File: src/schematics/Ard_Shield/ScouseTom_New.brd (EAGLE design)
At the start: 129.7 x 53.7 mm, 64 parts, among them IC1 LM317MBDT, IC2 AD5280, J1 Stim out Brd, J2 STIM OUT, Q1 FDV303N, Q2 BC817, Q3 FDN304P, U1 ADUM5402ARWZ, U2 ADM3202ARUZ, U3 ADUM5000ARWZ, U4 ADUM1410ARWZ, U5 ADUM1410ARWZ

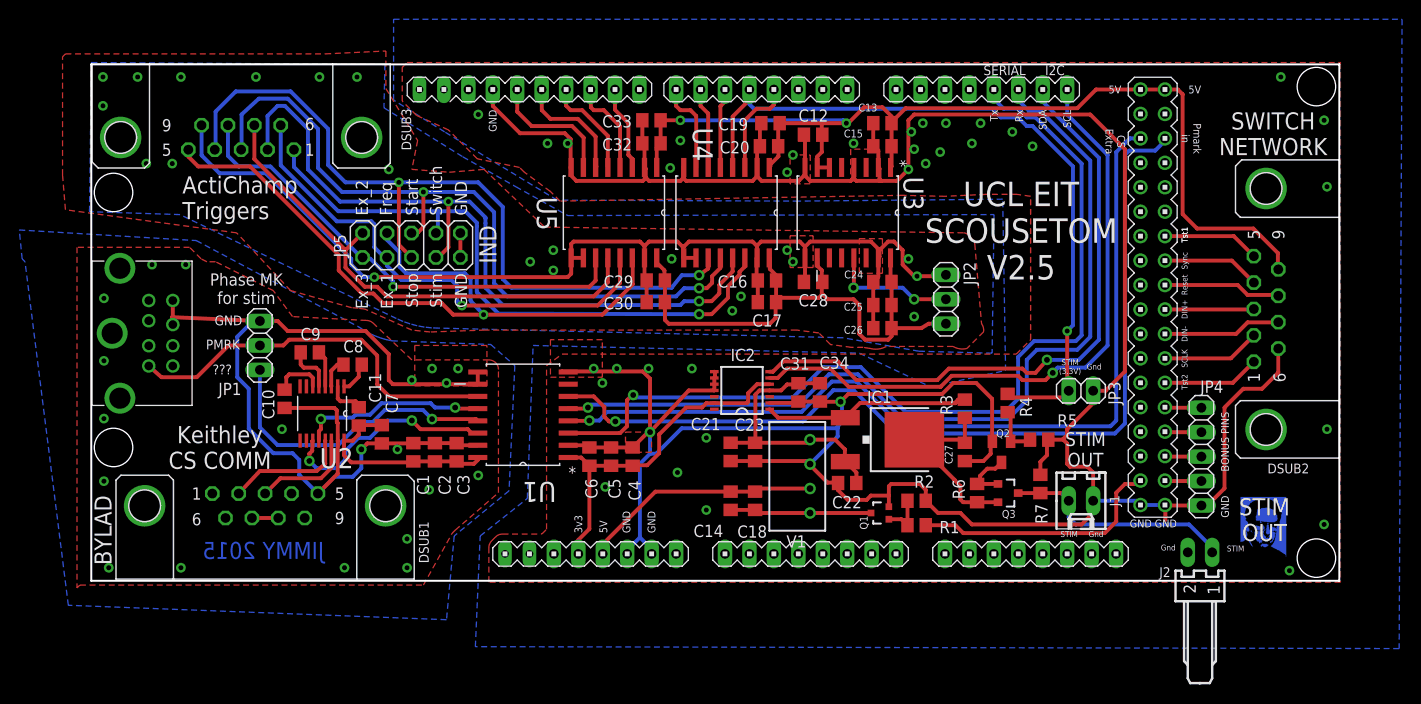
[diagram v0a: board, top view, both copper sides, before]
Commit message: Updated ScouseTom Shield SilkScreen and Gerber for PCB train order
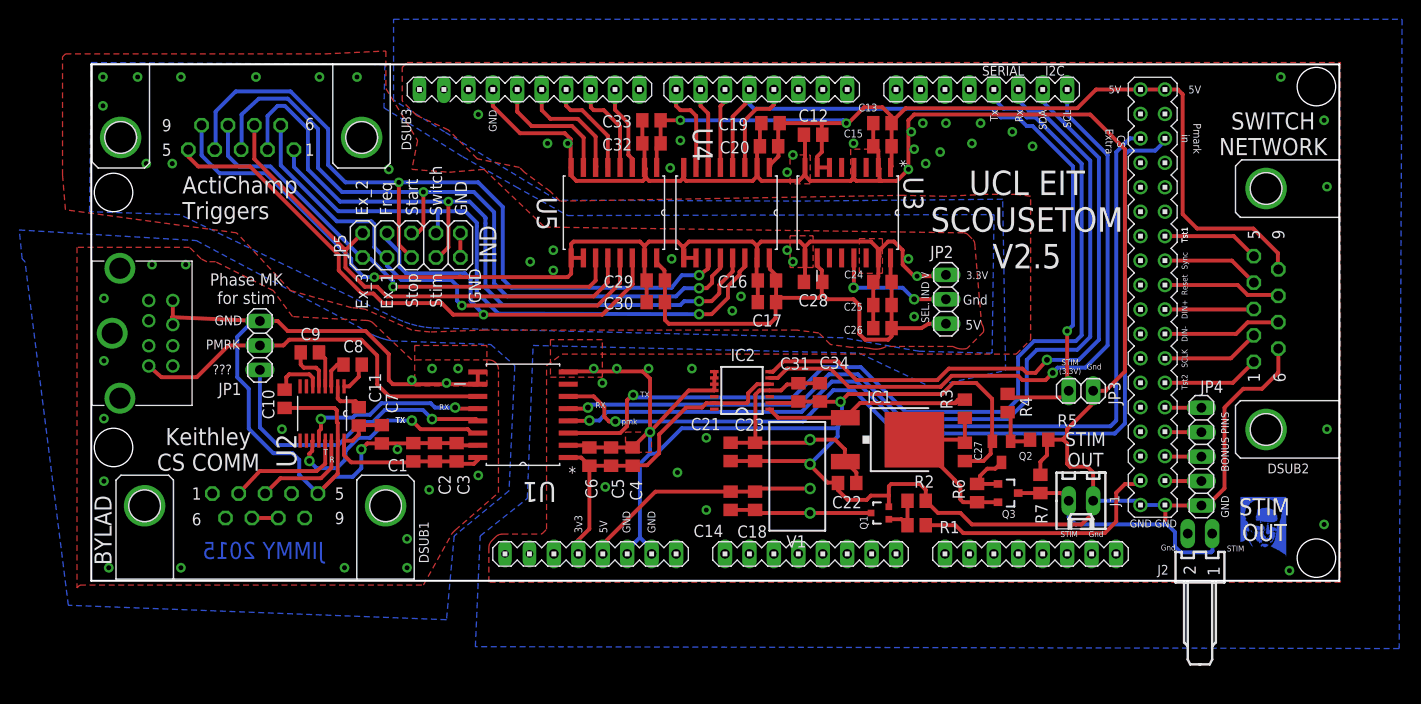
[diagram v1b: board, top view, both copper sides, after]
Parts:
- moved J2 1.95 mm to (99.9, 18.6)
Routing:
- net STIM_OUT: track 24.0 -> 26.5 mm
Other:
- board text added: "3.3V"
- board text added: "R"
- board text added: "RX"
- board text added: "SEL. IND V"
- board text added: "T"
- board text added: "TX"
- board text added: "pmk"

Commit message: CS extra pin added. Fixed angles on tracks
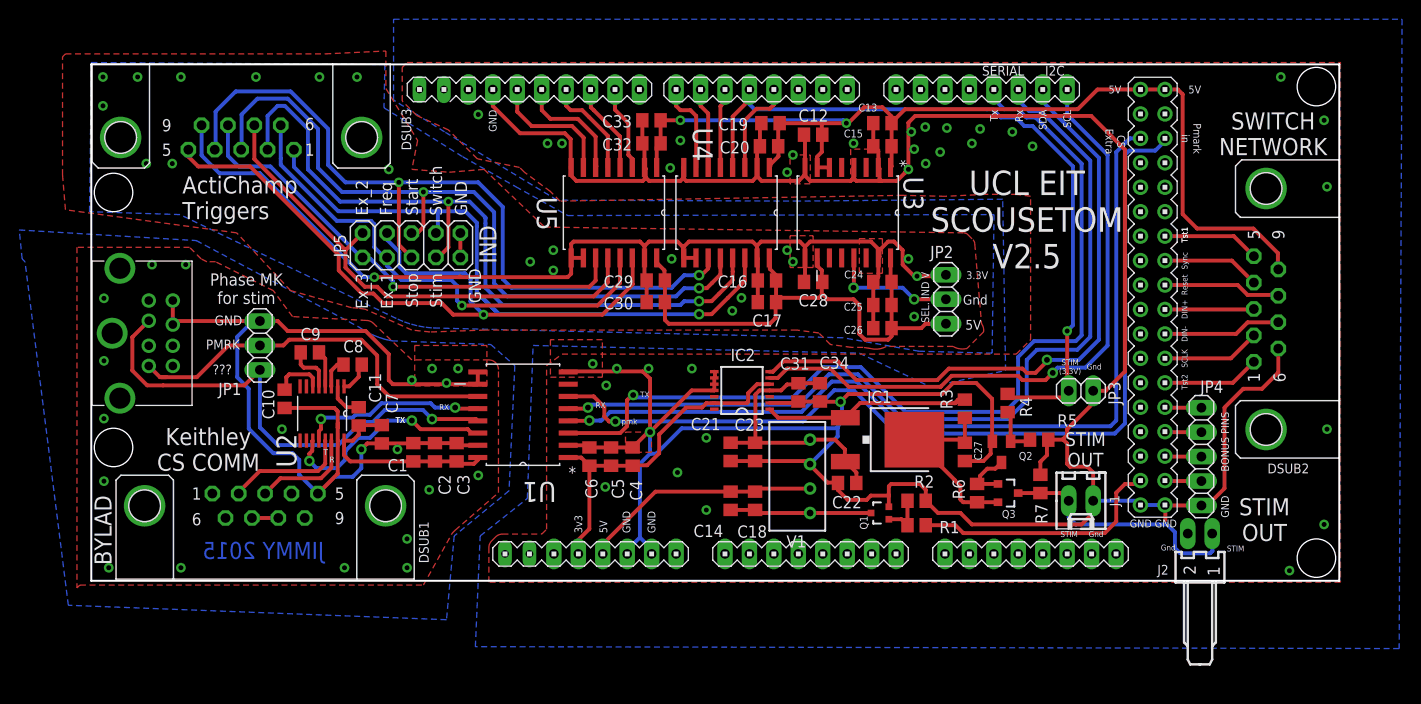
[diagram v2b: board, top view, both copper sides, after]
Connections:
- net CS_EXTRA_ISO: now also DIN1.2
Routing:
- net CS_EXTRA_ISO: track 31.4 -> 51.8 mm
- net IND_SWITCH_ISO: track 65.4 -> 67.6 mm
- net IND_EX_1: track 9.99 -> 9.37 mm
- net GND_ISO_TRIG: track 124.7 -> 124.2 mm
- net CS_PMARK_ISO: track 40.4 -> 41.0 mm

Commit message: Added pulldown resistors on CS and Switch board comm
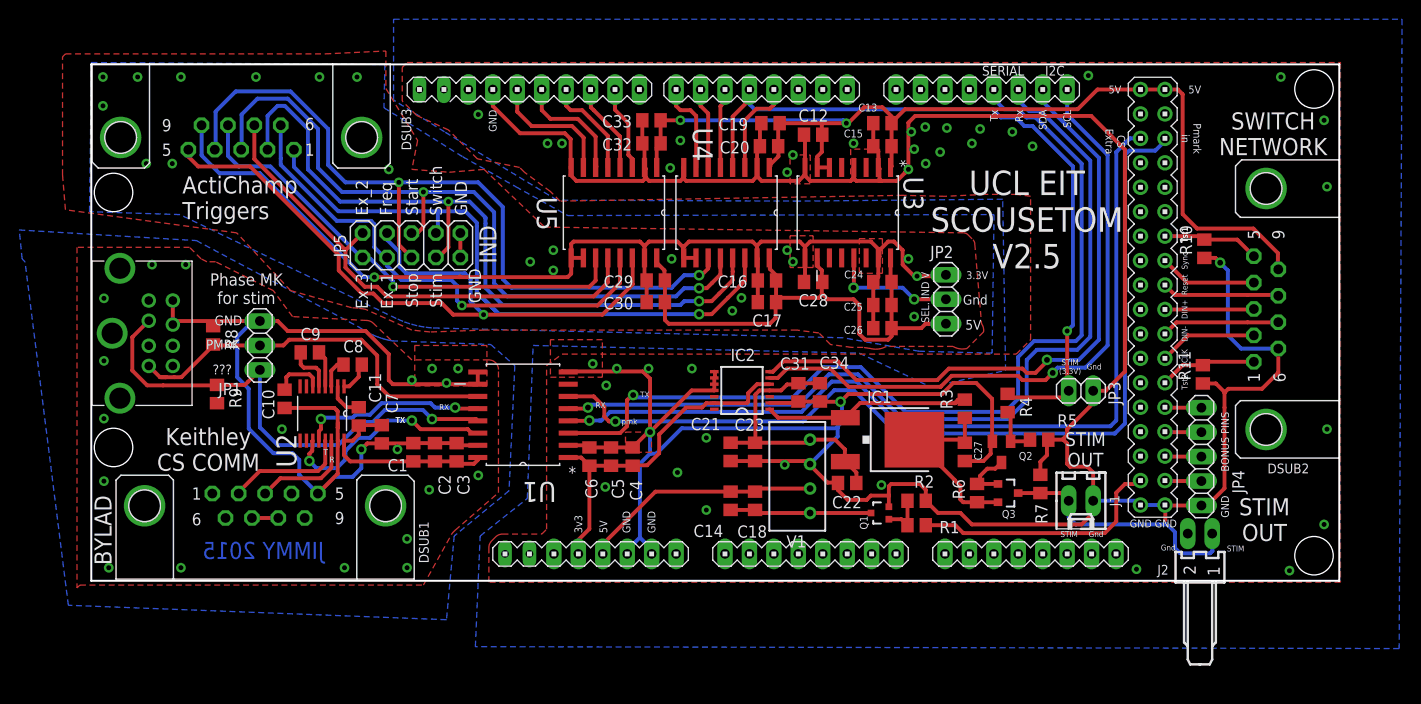
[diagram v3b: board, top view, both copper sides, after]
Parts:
- added R10, R11, R8, R9: 10k, resistor:R0805
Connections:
- net CS_EXTRA_ISO: now also R9.1
- net CS_PMARK_ISO: now also R8.2
- net GND: now also R10.1, R11.1
- net GND_ISO_RS232: now also R8.1, R9.2
- net TEST_1: now also R10.2
- net TEST_2: now also R11.2
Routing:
- net GND: track 350.0 -> 369.2 mm, vias 36 -> 41

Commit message: Updated Switchboard - pull down resistors, fixed routing, protection diodes and different battery connector
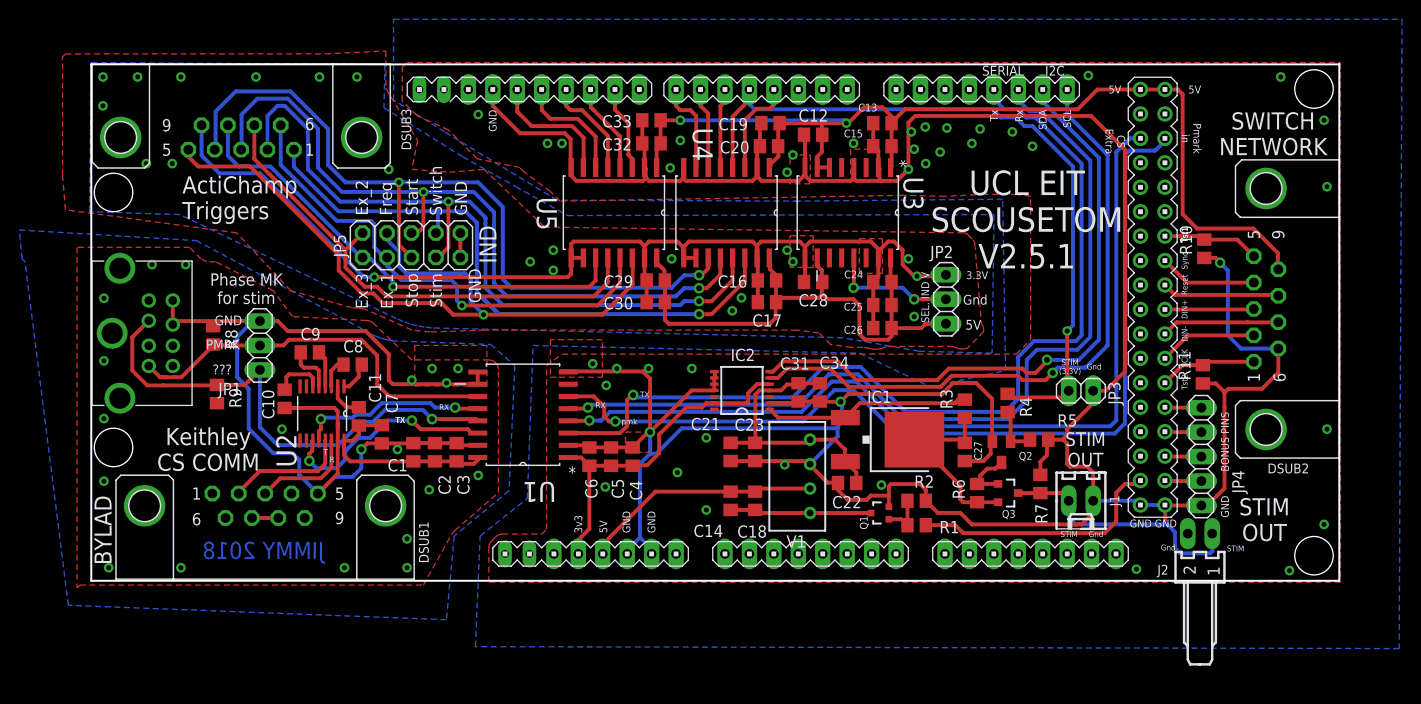
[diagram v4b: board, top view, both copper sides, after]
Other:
- board text added: "JIMMY 2018"
- board text added: "UCL EIT SCOUSETOM V2.5.1"
- board text removed: "JIMMY 2015"
- board text removed: "UCL EIT SCOUSETOM V2.5"
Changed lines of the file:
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@@
 <text x="81.91865" y="51.18725" size="2.54" layer="21" font="vector" ratio="21" align="center">UCL EIT
 SCOUSETOM
-V2.5</text>
+V2.5.1</text>
 <text x="-14.0928" y="18.9045" size="1.778" layer="21" font="vector" ratio="21" rot="R90" align="center">BYLAD</text>
-<text x="2.55" y="16.8" size="1.77" layer="16" font="vector" ratio="17" rot="MR0" align="center">JIMMY 2015</text>
+<text x="2.55" y="16.8" size="1.77" layer="16" font="vector" ratio="17" rot="MR0" align="center">JIMMY 2018</text>
 <dimension x1="-24.8" y1="67.2" x2="-24.892" y2="13.589" x3="-17.17976875" y3="40.38134375" textsize="1.77" textratio="17" layer="49"/>
 <dimension x1="-15.265" y1="67.31" x2="114.453" y2="67.31" x3="49.594" y3="74.9" textsize="1.77" textratio="17" layer="49"/>

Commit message: Gerbers for updated shield, sent to PCBtrain. Minor edits to routing
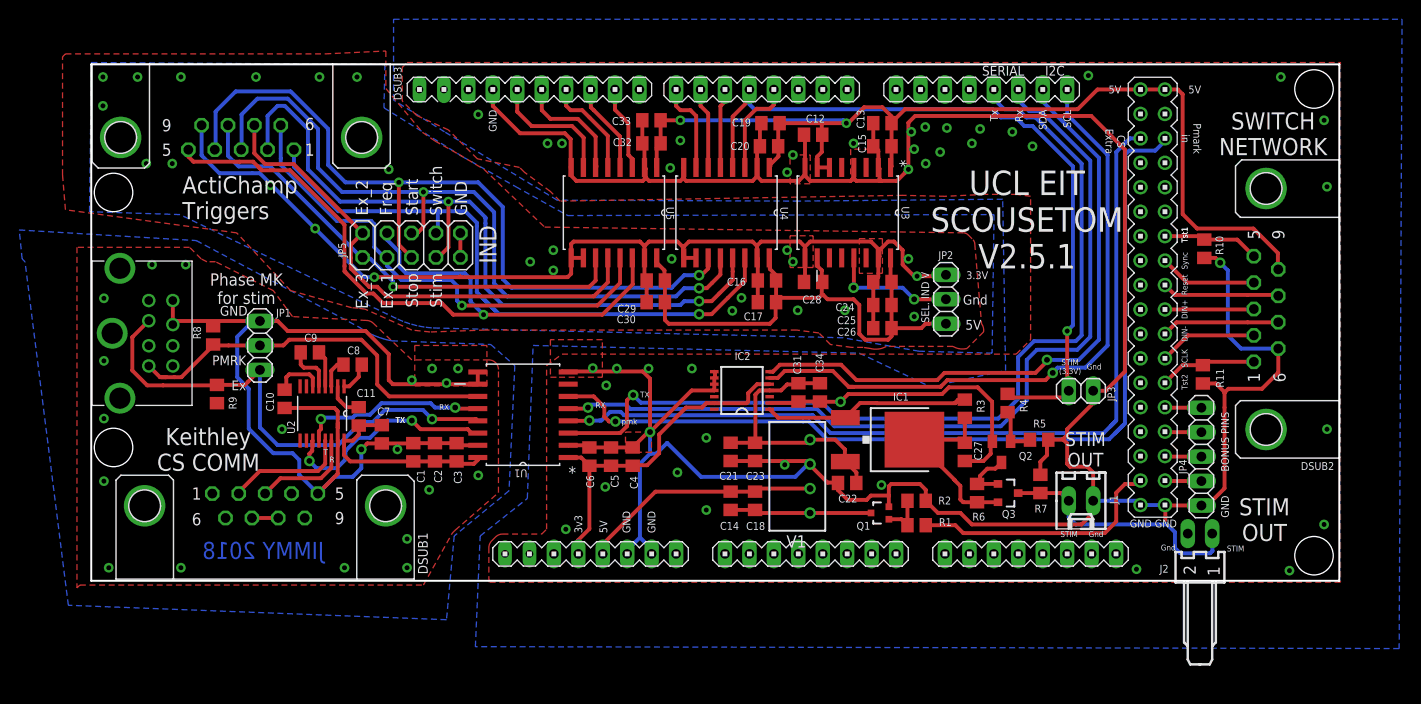
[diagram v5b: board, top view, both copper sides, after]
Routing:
- net GND: track 369.2 -> 359.4 mm, vias 41 -> 42
- net IND_FREQ_ISO: track 75.0 -> 77.1 mm
- net TTL_RX: track 93.2 -> 91.2 mm
- net TTL_TX: track 96.5 -> 94.7 mm
- net CS_EXTRA: track 91.8 -> 90.5 mm
- net CS_PMARK: track 96.1 -> 95.1 mm
- net GND_ISO_TRIG: vias 22 -> 26
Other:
- board text added: "Ex"
- board text removed: "???"
- board text removed: "BYLAD"
